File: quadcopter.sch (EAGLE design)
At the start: 75 parts, among them J1 ISP, J3 JUMPER, U2 ATMEGA128RFA1, Y1 16MHz

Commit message: Changed schematic slightly. Created basic board layout.
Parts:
- removed U$7: NET_BRIDGE, quadparts:NET_BRIDGE
- Q1, Q2, Q3, Q4, Q5, Q7: value (none) -> 2.6A
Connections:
- removed net N$1: C4.1, U$6.EN, U$6.IN, U$7.P$1
- net V_BAT: now also C4.1, U$6.EN, U$6.IN; no longer U$7.P$2
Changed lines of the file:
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@@
 <class number="0" name="default" width="0" drill="0">
+</class>
+<class number="1" name="RFSIG" width="0.4572" drill="0">
+</class>
+<class number="2" name="HIGHCURRENT" width="0.4572" drill="0">
 </class>
 </classes>
@@
 <part name="R3" library="quadparts_prebuilt" deviceset="RESISTOR_" device="SMD-2012-0805-10K" value="10K"/>
 <part name="C8" library="quadparts_prebuilt" deviceset="CAPACITOR-NP_" device="SMD-2012-0805_CERAMIC-1UF" value="1uF"/>
-<part name="Q1" library="quadparts" deviceset="NMOS" device="-SI2302CDS"/>
+<part name="Q1" library="quadparts" deviceset="NMOS" device="-SI2302CDS" value="2.6A"/>
 <part name="U$2" library="quadparts_prebuilt" deviceset="MOTOR_PADS" device=""/>
 <part name="D2" library="quadparts_prebuilt" deviceset="DIODE-SCHOTTKY_" device="SMD-SOD123-360MV" value="360mV"/>
@@
 <part name="R7" library="quadparts_prebuilt" deviceset="RESISTOR_" device="SMD-2012-0805-10K" value="10K"/>
 <part name="C12" library="quadparts_prebuilt" deviceset="CAPACITOR-NP_" device="SMD-2012-0805_CERAMIC-1UF" value="1uF"/>
-<part name="Q2" library="quadparts" deviceset="NMOS" device="-SI2302CDS"/>
+<part name="Q2" library="quadparts" deviceset="NMOS" device="-SI2302CDS" value="2.6A"/>
 <part name="U$3" library="quadparts_prebuilt" deviceset="MOTOR_PADS" device=""/>
 <part name="D3" library="quadparts_prebuilt" deviceset="DIODE-SCHOTTKY_" device="SMD-SOD123-360MV" value="360mV"/>
@@
 <part name="R9" library="quadparts_prebuilt" deviceset="RESISTOR_" device="SMD-2012-0805-10K" value="10K"/>
 <part name="C14" library="quadparts_prebuilt" deviceset="CAPACITOR-NP_" device="SMD-2012-0805_CERAMIC-1UF" value="1uF"/>
-<part name="Q3" library="quadparts" deviceset="NMOS" device="-SI2302CDS"/>
+<part name="Q3" library="quadparts" deviceset="NMOS" device="-SI2302CDS" value="2.6A"/>
 <part name="U$4" library="quadparts_prebuilt" deviceset="MOTOR_PADS" device=""/>
 <part name="D4" library="quadparts_prebuilt" deviceset="DIODE-SCHOTTKY_" device="SMD-SOD123-360MV" value="360mV"/>
@@
 <part name="R11" library="quadparts_prebuilt" deviceset="RESISTOR_" device="SMD-2012-0805-10K" value="10K"/>
 <part name="C17" library="quadparts_prebuilt" deviceset="CAPACITOR-NP_" device="SMD-2012-0805_CERAMIC-1UF" value="1uF"/>
-<part name="Q4" library="quadparts" deviceset="NMOS" device="-SI2302CDS"/>
+<part name="Q4" library="quadparts" deviceset="NMOS" device="-SI2302CDS" value="2.6A"/>
 <part name="P+5" library="quadparts_prebuilt" deviceset="VCC" device="" value="V_BAT"/>
 <part name="P+6" library="quadparts_prebuilt" deviceset="VCC" device="" value="V_BAT"/>
@@
 <part name="P+9" library="quadparts_prebuilt" deviceset="VCC" device="" value="V_BAT"/>
 <part name="U$6" library="quadparts_prebuilt" deviceset="TPS73633-DBVT" device="" value="LP3985"/>
-<part name="U$7" library="quadparts" deviceset="NET_BRIDGE" device=""/>
 <part name="C3" library="quadparts_prebuilt" deviceset="CAPACITOR-NP_" device="SMD-2012-0805_CERAMIC-1UF" value="1uF"/>
 <part name="GND20" library="quadparts_prebuilt" deviceset="BAT_GND" device=""/>
@@
 <part name="C13" library="quadparts_prebuilt" deviceset="CAPACITOR-POL_" device="SMD-7043-D_TANTALUM-220UF" value="220uF"/>
 <part name="C16" library="quadparts_prebuilt" deviceset="CAPACITOR-POL_" device="SMD-7043-D_TANTALUM-220UF" value="220uF"/>
-<part name="Q5" library="quadparts" deviceset="NMOS" device="-SI2302CDS"/>
-<part name="Q7" library="quadparts" deviceset="NMOS" device="-SI2302CDS"/>
+<part name="Q5" library="quadparts" deviceset="NMOS" device="-SI2302CDS" value="2.6A"/>
+<part name="Q7" library="quadparts" deviceset="NMOS" device="-SI2302CDS" value="2.6A"/>
 <part name="GND28" library="quadparts_prebuilt" deviceset="BAT_GND" device=""/>
 <part name="GND36" library="quadparts_prebuilt" deviceset="BAT_GND" device=""/>
@@
 <instance part="P+9" gate="VCC" x="-111.76" y="-63.5" rot="R180"/>
 <instance part="U$6" gate="G$1" x="-111.76" y="-101.6"/>
-<instance part="U$7" gate="G$1" x="-116.84" y="-55.88"/>
 <instance part="C3" gate="G$1" x="-76.2" y="-91.44"/>
 <instance part="GND20" gate="1" x="-86.36" y="-63.5"/>
@@
 </segment>
 </net>
-<net name="RFANT" class="0">
+<net name="RFANT" class="1">
 <segment>
 <wire x1="144.78" y1="63.5" x2="157.48" y2="63.5" width="0.1524" layer="91"/>
@@
 </segment>
 </net>
-<net name="FLYBACK_BR" class="0">
+<net name="FLYBACK_BR" class="2">
 <segment>
 <pinref part="D3" gate="G$1" pin="A"/>
@@
 </segment>
 </net>
-<net name="FLYBACK_TL" class="0">
+<net name="FLYBACK_TL" class="2">
 <segment>
 <pinref part="D2" gate="G$1" pin="A"/>
@@
 </segment>
 </net>
-<net name="FLYBACK_TR" class="0">
+<net name="FLYBACK_TR" class="2">
 <segment>
 <pinref part="D1" gate="G$1" pin="A"/>
@@
 </segment>
 </net>
-<net name="FLYBACK_BL" class="0">
+<net name="FLYBACK_BL" class="2">
 <segment>
 <pinref part="D4" gate="G$1" pin="A"/>
@@
 </segment>
 </net>
-<net name="V_BAT" class="0">
+<net name="V_BAT" class="2">
 <segment>
 <wire x1="-106.68" y1="83.82" x2="-106.68" y2="86.36" width="0.1524" layer="91"/>
@@
 </segment>
 <segment>
-<pinref part="U$7" gate="G$1" pin="P$2"/>
 <pinref part="P+9" gate="VCC" pin="VCC"/>
 <wire x1="-111.76" y1="-60.96" x2="-111.76" y2="-55.88" width="0.1524" layer="91"/>
 <pinref part="J3" gate="G$1" pin="1"/>
 <wire x1="-109.22" y1="-55.88" x2="-111.76" y2="-55.88" width="0.1524" layer="91"/>
+<wire x1="-121.92" y1="-55.88" x2="-121.92" y2="-88.9" width="0.1524" layer="91"/>
+<pinref part="U$6" gate="G$1" pin="IN"/>
+<wire x1="-121.92" y1="-88.9" x2="-114.3" y2="-88.9" width="0.1524" layer="91"/>
+<wire x1="-121.92" y1="-88.9" x2="-132.08" y2="-88.9" width="0.1524" layer="91"/>
+<wire x1="-132.08" y1="-88.9" x2="-132.08" y2="-93.98" width="0.1524" layer="91"/>
+<junction x="-121.92" y="-88.9"/>
+<pinref part="C4" gate="G$1" pin="1"/>
+<pinref part="U$6" gate="G$1" pin="EN"/>
+<wire x1="-114.3" y1="-99.06" x2="-121.92" y2="-99.06" width="0.1524" layer="91"/>
+<wire x1="-121.92" y1="-99.06" x2="-121.92" y2="-88.9" width="0.1524" layer="91"/>
+<wire x1="-121.92" y1="-55.88" x2="-111.76" y2="-55.88" width="0.1524" layer="91"/>
 <junction x="-111.76" y="-55.88"/>
 </segment>
 </net>
-<net name="BAT_GND" class="0">
+<net name="BAT_GND" class="2">
 <segment>
 <pinref part="J2" gate="G$1" pin="9"/>
@@
 </segment>
 </net>
-<net name="N$1" class="0">
-<segment>
-<pinref part="U$7" gate="G$1" pin="P$1"/>
-<wire x1="-121.92" y1="-55.88" x2="-121.92" y2="-88.9" width="0.1524" layer="91"/>
-<pinref part="U$6" gate="G$1" pin="IN"/>
-<wire x1="-121.92" y1="-88.9" x2="-114.3" y2="-88.9" width="0.1524" layer="91"/>
-<wire x1="-121.92" y1="-88.9" x2="-132.08" y2="-88.9" width="0.1524" layer="91"/>
-<wire x1="-132.08" y1="-88.9" x2="-132.08" y2="-93.98" width="0.1524" layer="91"/>
-<junction x="-121.92" y="-88.9"/>
-<pinref part="C4" gate="G$1" pin="1"/>
-<pinref part="U$6" gate="G$1" pin="EN"/>
-<wire x1="-114.3" y1="-99.06" x2="-121.92" y2="-99.06" width="0.1524" layer="91"/>
-<wire x1="-121.92" y1="-99.06" x2="-121.92" y2="-88.9" width="0.1524" layer="91"/>
-</segment>
-</net>
 <net name="N$5" class="0">
 <segment>
@@
 </segment>
 </net>
-<net name="N$6" class="0">
+<net name="N$6" class="2">
 <segment>
 <pinref part="Q5" gate="G$1" pin="D"/>
@@
 </segment>
 </net>
-<net name="N$10" class="0">
+<net name="N$10" class="2">
 <segment>
 <pinref part="Q7" gate="G$1" pin="D"/>
@@
 </segment>
 </net>
-<net name="N$11" class="0">
+<net name="N$11" class="2">
 <segment>
 <wire x1="160.02" y1="-55.88" x2="162.56" y2="-55.88" width="0.1524" layer="91"/>
@@
 </segment>
 </net>
-<net name="N$12" class="0">
+<net name="N$12" class="2">
 <segment>
 <wire x1="160.02" y1="-68.58" x2="162.56" y2="-68.58" width="0.1524" layer="91"/>
@@
 </segment>
 </net>
-<net name="N$15" class="0">
+<net name="N$15" class="2">
 <segment>
 <wire x1="160.02" y1="-93.98" x2="162.56" y2="-93.98" width="0.1524" layer="91"/>
@@
 </segment>
 </net>
-<net name="N$16" class="0">
+<net name="N$16" class="2">
 <segment>
 <wire x1="160.02" y1="-106.68" x2="162.56" y2="-106.68" width="0.1524" layer="91"/>
@@
 </segment>
 </net>
-<net name="N$2" class="0">
+<net name="N$2" class="2">
 <segment>
 <pinref part="J3" gate="G$1" pin="2"/>

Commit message: Corrected mistakes found on schematics and libraries. Rerouted board from updated schematic.
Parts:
- removed R14, R16: 10K, quadparts_prebuilt:RESISTOR_SMD-2012-0805-10K
- C12, C14, C17, C8: value 1uF -> 0.1uF; device quadparts_prebuilt:CAPACITOR-NP_SMD-2012-0805_CERAMIC-1UF -> quadparts_prebuilt:CAPACITOR-NP_SMD-2012-0805_CERAMIC-0.1UF
- R12, R13: value 330 -> 10K; device quadparts_prebuilt:RESISTOR_SMD-2012-0805-330 -> quadparts_prebuilt:RESISTOR_SMD-2012-0805-10K
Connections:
- net BAT_GND: now also C4.2, U$6.GND; no longer R14.1, R16.1
- net FILTERED_BL: now also C17.2, R4.2; no longer R10.2
- net FILTERED_BR: now also C14.2
- net FILTERED_TL: now also C12.2, R2.2; no longer R4.2
- net FILTERED_TR: now also C8.2, R10.2; no longer R2.2
- net GND: no longer C4.2, U$6.GND
- net LED_B: no longer R14.2
- net LED_R: no longer R16.2
- net PWM_BL: now also R4.1; no longer C17.2, R10.1
- net PWM_BR: no longer C14.2
- net PWM_TL: now also R2.1; no longer C12.2, R4.1
- net PWM_TR: now also R10.1; no longer C8.2, R2.1
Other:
- moved on the sheet: R10, R2, R4, R8

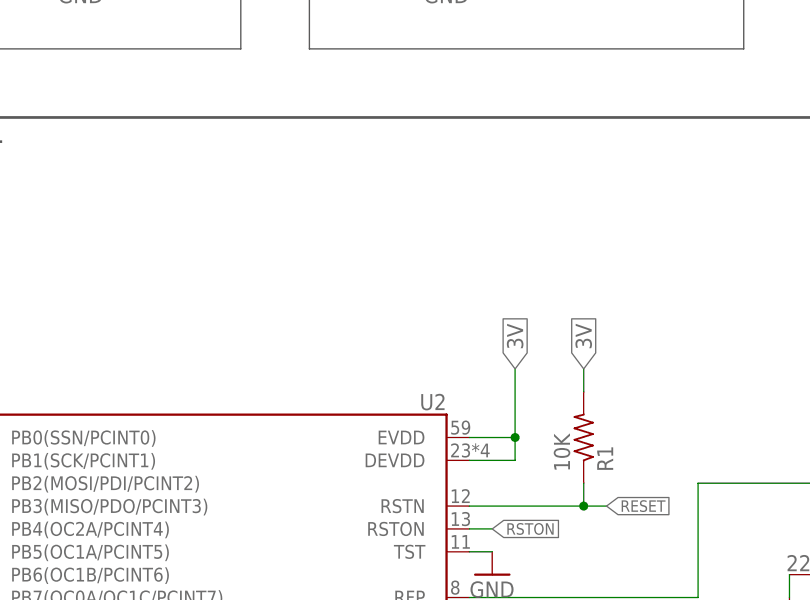
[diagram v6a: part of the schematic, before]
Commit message: Updated board and cam to meet new board review changes.
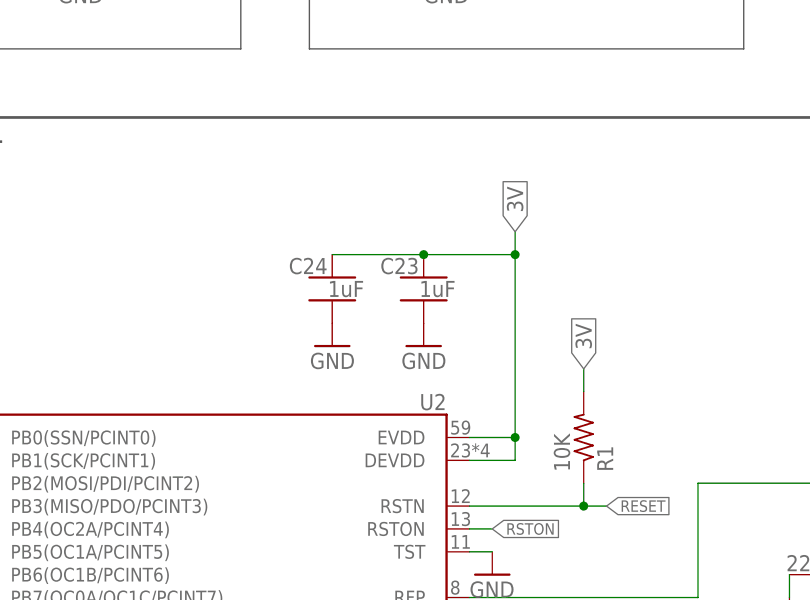
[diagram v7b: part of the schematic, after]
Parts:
- added C23, C24: 1uF, quadparts_prebuilt:CAPACITOR-NP_SMD-2012-0805_CERAMIC-1UF
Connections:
- net 3V: now also C23.1, C24.1
- net GND: now also C23.2, C24.2
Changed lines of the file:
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@@
 <part name="R8" library="quadparts_prebuilt" deviceset="RESISTOR_" device="SMD-2012-0805-100" value="100"/>
 <part name="R10" library="quadparts_prebuilt" deviceset="RESISTOR_" device="SMD-2012-0805-100" value="100"/>
+<part name="C23" library="quadparts_prebuilt" deviceset="CAPACITOR-NP_" device="SMD-2012-0805_CERAMIC-1UF" value="1uF"/>
+<part name="C24" library="quadparts_prebuilt" deviceset="CAPACITOR-NP_" device="SMD-2012-0805_CERAMIC-1UF" value="1uF"/>
+<part name="GND35" library="quadparts_prebuilt" deviceset="GND" device=""/>
+<part name="GND37" library="quadparts_prebuilt" deviceset="GND" device=""/>
 </parts>
 <sheets>
@@
 <instance part="R8" gate="G$1" x="-58.42" y="-10.16"/>
 <instance part="R10" gate="G$1" x="-43.18" y="53.34"/>
+<instance part="C23" gate="G$1" x="83.82" y="86.36" rot="MR0"/>
+<instance part="C24" gate="G$1" x="73.66" y="86.36" rot="MR0"/>
+<instance part="GND35" gate="1" x="73.66" y="78.74" rot="MR0"/>
+<instance part="GND37" gate="1" x="83.82" y="78.74" rot="MR0"/>
 </instances>
 <busses>
@@
 <junction x="48.26" y="-91.44"/>
 </segment>
+<segment>
+<pinref part="C24" gate="G$1" pin="2"/>
+<pinref part="GND35" gate="1" pin="GND"/>
+</segment>
+<segment>
+<pinref part="C23" gate="G$1" pin="2"/>
+<pinref part="GND37" gate="1" pin="GND"/>
+</segment>
 </net>
 <net name="N$3" class="0">
@@
 <segment>
 <wire x1="88.9" y1="68.58" x2="93.98" y2="68.58" width="0.1524" layer="91"/>
-<wire x1="93.98" y1="68.58" x2="93.98" y2="76.2" width="0.1524" layer="91"/>
+<wire x1="93.98" y1="68.58" x2="93.98" y2="88.9" width="0.1524" layer="91"/>
+<wire x1="93.98" y1="88.9" x2="93.98" y2="91.44" width="0.1524" layer="91"/>
 <wire x1="88.9" y1="66.04" x2="93.98" y2="66.04" width="0.1524" layer="91"/>
 <wire x1="93.98" y1="66.04" x2="93.98" y2="68.58" width="0.1524" layer="91"/>
@@
 <pinref part="U2" gate="G$1" pin="DEVDD"/>
 <pinref part="U2" gate="G$1" pin="EVDD"/>
-<label x="93.98" y="76.2" size="1.778" layer="95" rot="R90" xref="yes"/>
-</segment>
-<segment>
+<label x="93.98" y="91.44" size="1.778" layer="95" rot="R90" xref="yes"/>
+<pinref part="C23" gate="G$1" pin="1"/>
+<wire x1="93.98" y1="88.9" x2="83.82" y2="88.9" width="0.1524" layer="91"/>
+<junction x="93.98" y="88.9"/>
+<pinref part="C24" gate="G$1" pin="1"/>
+<wire x1="83.82" y1="88.9" x2="73.66" y2="88.9" width="0.1524" layer="91"/>
+<junction x="83.82" y="88.9"/>
+</segment>
+<segment>

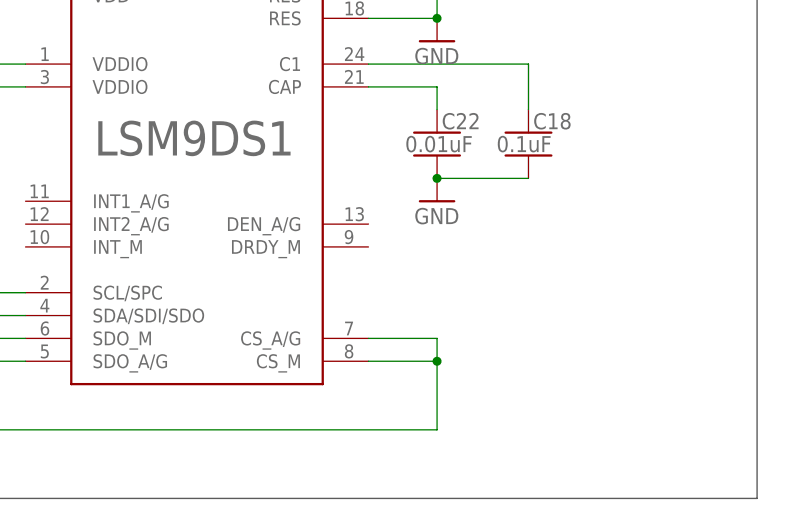
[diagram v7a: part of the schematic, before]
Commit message: Completed board routing
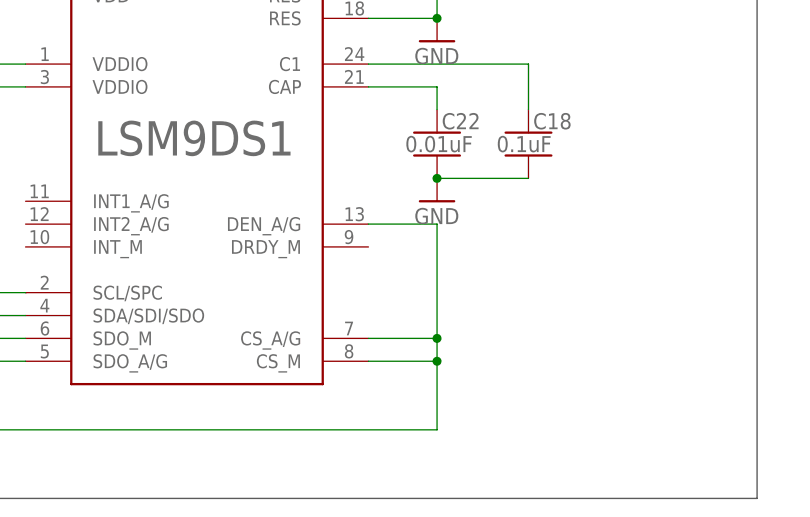
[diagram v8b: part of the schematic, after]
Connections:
- net 3V: now also LSM9DS1.DEN_A/G
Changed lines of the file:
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@@
 <junction x="-10.16" y="-81.28"/>
 <label x="-30.48" y="-81.28" size="1.778" layer="95" rot="R180" xref="yes"/>
+<pinref part="LSM9DS1" gate="G$1" pin="DEN_A/G"/>
+<wire x1="40.64" y1="-96.52" x2="48.26" y2="-96.52" width="0.1524" layer="91"/>
+<wire x1="48.26" y1="-96.52" x2="48.26" y2="-109.22" width="0.1524" layer="91"/>
+<junction x="48.26" y="-109.22"/>
 </segment>
 </net>
